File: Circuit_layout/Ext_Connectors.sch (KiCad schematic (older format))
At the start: 13 parts, among them CON1 AVR-JTAG-10, J1 CONN_01X03, J10 CONN_01X02, J11 CONN_8, J2 CONN_01X03, J3 CONN_01X02, J4 CONN_01X04, J5 RJ12, J6 CONN_01X02, J7 CONN_01X06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

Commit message: working on schematic
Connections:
- net labels added: Brake_Light_RTN
- wire segments 63 -> 66
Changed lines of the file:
@@
 EESchema Schematic File Version 2
 LIBS:Circuit_layout-rescue
+LIBS:TSI_KiCad_Lib
 LIBS:TSI_HV_Isolater-cache
 LIBS:74xgxx
@@
 	1    0    0    -1
 $EndComp
-Text Label 9250 1700 0    60   ~ 0
-LV_GND
-Text Label 9250 1800 0    60   ~ 0
-Brake_Light
 Text Label 9250 1900 0    60   ~ 0
 HVPL_1
@@
 	9850 3000 9100 3000
 Wire Wire Line
-	9850 2200 9250 2200
+	8850 2200 9850 2200
 Wire Wire Line
 	9850 2100 9250 2100
 Wire Wire Line
-	9850 2000 9250 2000
+	8850 2000 9850 2000
 Wire Wire Line
 	9850 1900 9250 1900
 Wire Wire Line
-	9850 1800 9250 1800
-Wire Wire Line
-	9850 1700 9250 1700
+	8550 1800 9850 1800
+Wire Wire Line
+	9850 1700 9150 1700
 Wire Wire Line
 	9950 1400 9350 1400
@@
 	9850 2300 9250 2300
 Wire Wire Line
-	9850 2400 9250 2400
+	9100 2400 9850 2400
 Text GLabel 2050 6400 2    60   Input ~ 0
 Throttle_RTN
@@
 	5750 5450 6100 5450
 Wire Wire Line
-	6100 5050 6100 5550
+	6100 5050 6100 5450
+Wire Wire Line
+	6100 5450 6100 5550
 Wire Wire Line
 	5750 5050 6100 5050
@@
 Wire Wire Line
 	9350 900  9950 900
+Text GLabel 9300 4350 0    60   Input ~ 0
+AIRs-_in
+Text GLabel 9300 4450 0    60   Input ~ 0
+AIRs+_in
+Wire Wire Line
+	9100 2400 9100 2450
+$Comp
+L GND #PWR?
+U 1 1 58B3D38F
+P 9100 2450
+F 0 "#PWR?" H 9100 2200 50  0001 C CNN
+F 1 "GND" H 9100 2300 50  0000 C CNN
+F 2 "" H 9100 2450 50  0000 C CNN
+F 3 "" H 9100 2450 50  0000 C CNN
+	1    9100 2450
+	1    0    0    -1
+$EndComp
+Text GLabel 9150 1700 0    60   Input ~ 0
+Brake_Light
+Text Label 9150 1800 0    60   ~ 0
+Brake_Light_RTN
+$Comp
+L GND #PWR?
+U 1 1 58B41C25
+P 8550 1800
+F 0 "#PWR?" H 8550 1550 50  0001 C CNN
+F 1 "GND" H 8550 1650 50  0000 C CNN
+F 2 "" H 8550 1800 50  0000 C CNN
+F 3 "" H 8550 1800 50  0000 C CNN
+	1    8550 1800
+	1    0    0    -1
+$EndComp
+Wire Wire Line
+	8850 2200 8850 2200
+$Comp
+L GND #PWR?
+U 1 1 58B4A72F
+P 8850 2000
+F 0 "#PWR?" H 8850 1750 50  0001 C CNN
+F 1 "GND" H 8850 1850 50  0000 C CNN
+F 2 "" H 8850 2000 50  0000 C CNN
+F 3 "" H 8850 2000 50  0000 C CNN
+	1    8850 2000
+	1    0    0    -1
+$EndComp
+$Comp
+L GND #PWR?
+U 1 1 58B4A794
+P 8850 2200
+F 0 "#PWR?" H 8850 1950 50  0001 C CNN
+F 1 "GND" H 8850 2050 50  0000 C CNN
+F 2 "" H 8850 2200 50  0000 C CNN
+F 3 "" H 8850 2200 50  0000 C CNN
+	1    8850 2200
+	1    0    0    -1
+$EndComp
 $EndSCHEMATC

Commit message: added TSMP
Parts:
- added P?: CONN_01X02, symbol CONN_01X02
- added R? (x2): 10k, symbol R
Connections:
- net labels added: TSMP+, TSMP-
- wire segments 66 -> 70
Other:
- note added: "5W Resistor for TSMP\n(20.47mm x 9.27mm)\nNeed footprint"
- note added: "TSMP"
- moved on the sheet: J4, P1

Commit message: took notes w/ greg
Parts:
- gave numbers to parts that had none: 3
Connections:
- net labels removed: Earth
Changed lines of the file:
@@
 Text GLabel 9350 6150 0    60   Input ~ 0
 LVRTN
-$Comp
-L Earth #PWR018
-U 1 1 58AF0E42
-P 9350 6250
-F 0 "#PWR018" H 9350 6000 50  0001 C CNN
-F 1 "Earth" H 9350 6100 50  0001 C CNN
-F 2 "" H 9350 6250 50  0000 C CNN
-F 3 "" H 9350 6250 50  0000 C CNN
-	1    9350 6250
-	1    0    0    -1
-$EndComp
 Text Label 9350 6050 0    60   ~ 0
 24_GLV
 $Comp
-L +24V #PWR019
+L +24V #PWR018
 U 1 1 58AF1C5B
 P 9100 5900
-F 0 "#PWR019" H 9100 5750 50  0001 C CNN
+F 0 "#PWR018" H 9100 5750 50  0001 C CNN
 F 1 "+24V" H 9100 6040 50  0000 C CNN
 F 2 "" H 9100 5900 50  0000 C CNN
@@
 Drive_LED
 $Comp
-L +5V #PWR020
+L +5V #PWR019
 U 1 1 58B1052B
 P 8450 3000
-F 0 "#PWR020" H 8450 2850 50  0001 C CNN
+F 0 "#PWR019" H 8450 2850 50  0001 C CNN
 F 1 "+5V" H 8450 3140 50  0000 C CNN
 F 2 "" H 8450 3000 50  0000 C CNN
@@
 AIRs+_in
 $Comp
-L GND #PWR?
+L GND #PWR020
 U 1 1 58B3D38F
 P 9100 2450
-F 0 "#PWR?" H 9100 2200 50  0001 C CNN
+F 0 "#PWR020" H 9100 2200 50  0001 C CNN
 F 1 "GND" H 9100 2300 50  0000 C CNN
 F 2 "" H 9100 2450 50  0000 C CNN
@@
 Brake_Light_RTN
 $Comp
-L GND #PWR?
+L GND #PWR021
 U 1 1 58B41C25
 P 8550 1800
-F 0 "#PWR?" H 8550 1550 50  0001 C CNN
+F 0 "#PWR021" H 8550 1550 50  0001 C CNN
 F 1 "GND" H 8550 1650 50  0000 C CNN
 F 2 "" H 8550 1800 50  0000 C CNN
@@
 $EndComp
 $Comp
-L GND #PWR?
+L GND #PWR022
 U 1 1 58B4A72F
 P 8850 2000
-F 0 "#PWR?" H 8850 1750 50  0001 C CNN
+F 0 "#PWR022" H 8850 1750 50  0001 C CNN
 F 1 "GND" H 8850 1850 50  0000 C CNN
 F 2 "" H 8850 2000 50  0000 C CNN
@@
 $EndComp
 $Comp
-L GND #PWR?
+L GND #PWR023
 U 1 1 58B4A794
 P 8850 2200
-F 0 "#PWR?" H 8850 1950 50  0001 C CNN
+F 0 "#PWR023" H 8850 1950 50  0001 C CNN
 F 1 "GND" H 8850 2050 50  0000 C CNN
 F 2 "" H 8850 2200 50  0000 C CNN
@@
 $EndComp
 $Comp
-L R R?
+L R R8
 U 1 1 58B4665F
 P 2600 7300
-F 0 "R?" V 2680 7300 50  0000 C CNN
+F 0 "R8" V 2680 7300 50  0000 C CNN
 F 1 "10k" V 2600 7300 50  0000 C CNN
 F 2 "" V 2530 7300 50  0001 C CNN
@@
 TSMP
 $Comp
-L R R?
+L R R14
 U 1 1 58B47866
 P 2600 7600
-F 0 "R?" V 2680 7600 50  0000 C CNN
+F 0 "R14" V 2680 7600 50  0000 C CNN
 F 1 "10k" V 2600 7600 50  0000 C CNN
 F 2 "" V 2530 7600 50  0001 C CNN
@@
 	2150 7600 2450 7600
 $Comp
-L CONN_01X02 P?
+L CONN_01X02 P2
 U 1 1 58B47ED4
 P 950 7400
-F 0 "P?" H 950 7550 50  0000 C CNN
+F 0 "P2" H 950 7550 50  0000 C CNN
 F 1 "CONN_01X02" V 1050 7400 50  0000 C CNN
 F 2 "" H 950 7400 50  0000 C CNN
@@
 Text Label 2150 7600 0    60   ~ 0
 TSMP-
+$Comp
+L GND #PWR024
+U 1 1 58B6646E
+P 9350 6250
+F 0 "#PWR024" H 9350 6000 50  0001 C CNN
+F 1 "GND" H 9350 6100 50  0000 C CNN
+F 2 "" H 9350 6250 50  0000 C CNN
+F 3 "" H 9350 6250 50  0000 C CNN
+	1    9350 6250
+	1    0    0    -1
+$EndComp
 $EndSCHEMATC

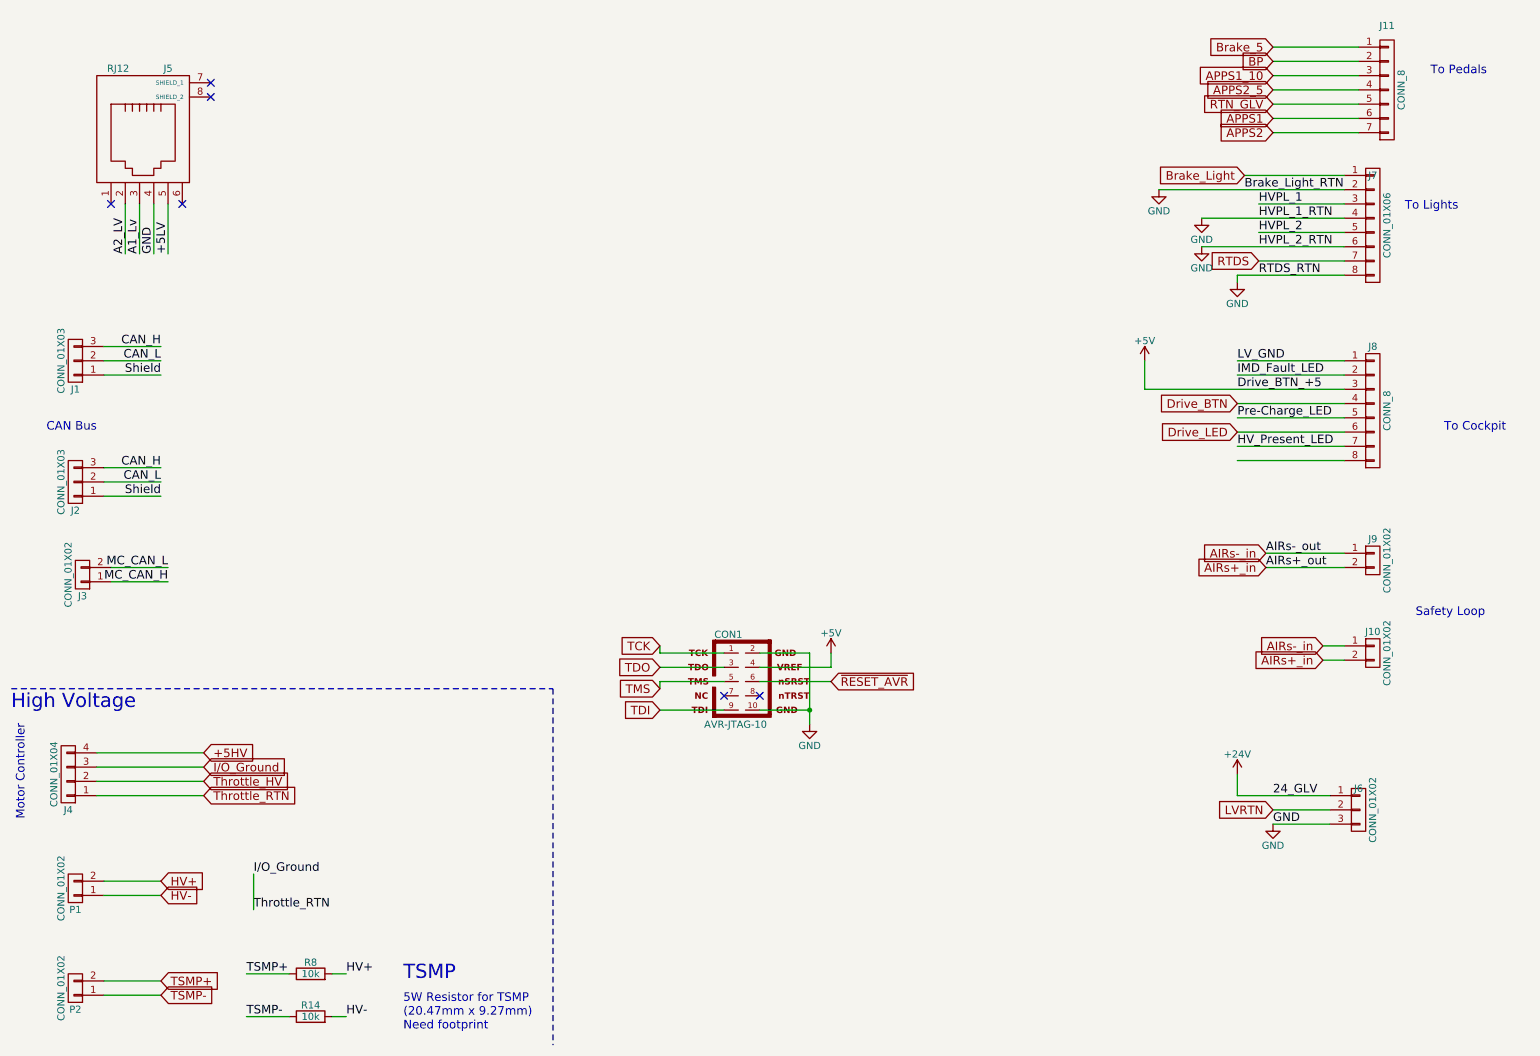
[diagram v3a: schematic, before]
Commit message: got rid of some warnings with nets.
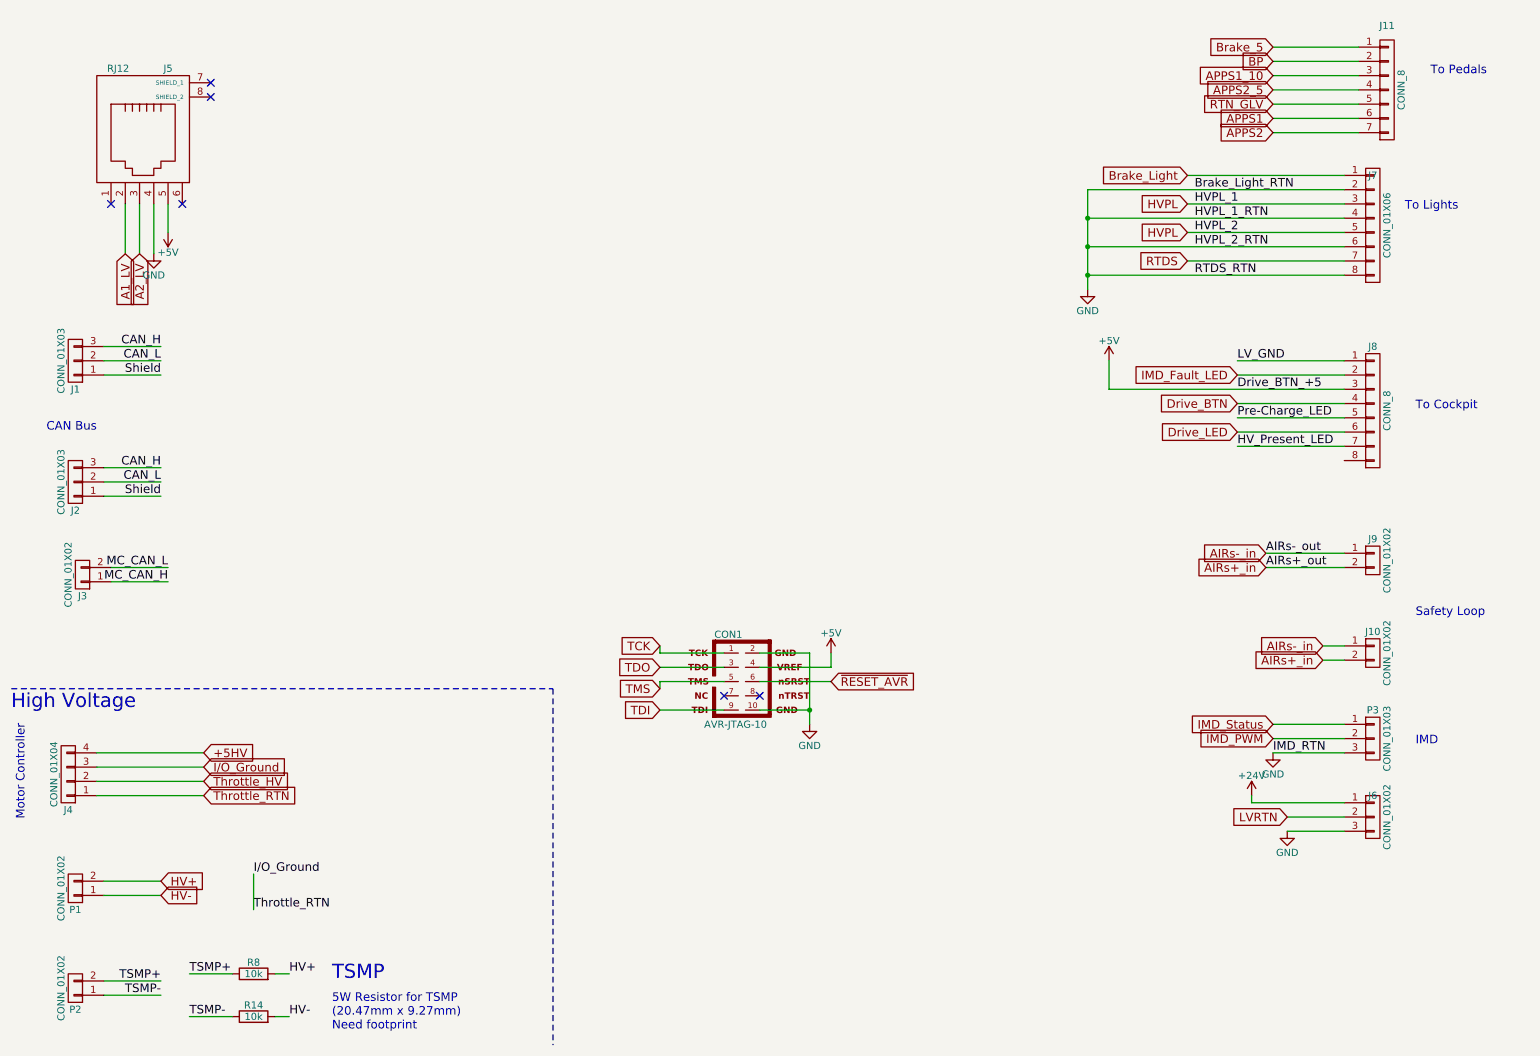
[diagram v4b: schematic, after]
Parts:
- added P3: CONN_01X03, symbol CONN_01X03
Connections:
- net +5LV is gone; now on net +5V: J5.5
- net A1_Lv is gone; now on net A2_LV: J5.3
- net HVPL_2 is gone; now on net HVPL: J7.5 (P5)
- net A2_LV: no longer J5.2
- net GND: now also P3.3 (P3)
- net HVPL_1 renamed HVPL
- new net A1_LV: J5.2
- new net IMD_PWM: P3.2 (P2)
- new net IMD_Status: P3.1 (P1)
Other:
- note added: "IMD"
- moved on the sheet: J6, R14, R8
